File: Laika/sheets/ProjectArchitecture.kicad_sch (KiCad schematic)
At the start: 0 parts

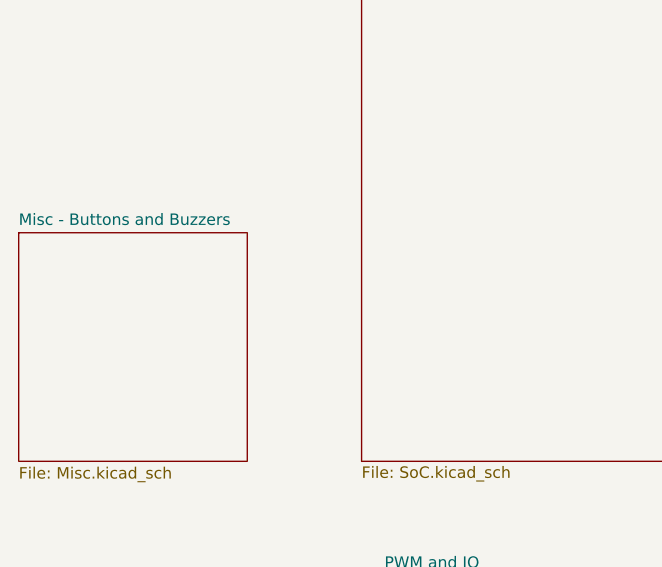
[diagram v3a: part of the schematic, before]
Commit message: Created misc. block
Populated sheet for misc. components. This includes three switches for
SoC bringup (update, reset, arm/risc-v select). Added buzzer and user
led.
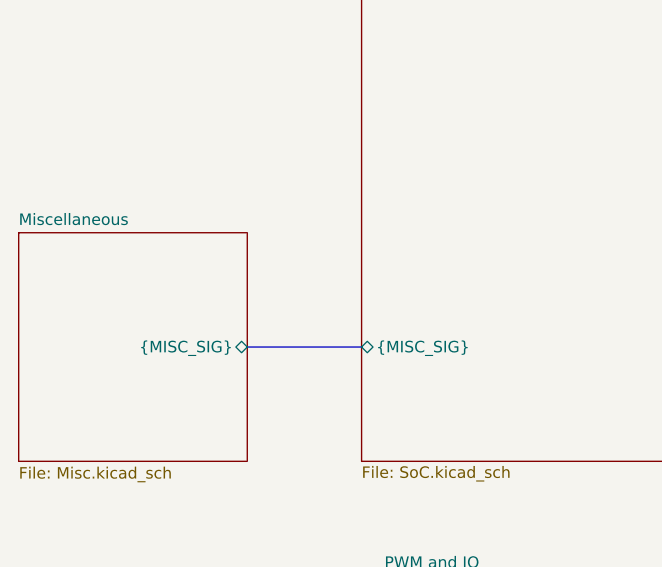
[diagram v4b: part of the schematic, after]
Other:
- sheet Misc - Buttons and Buzzers renamed Miscellaneous
- sheet Miscellaneous ports: added {MISC_SIG}; removed none
- sheet SoC ports: added {MISC_SIG}; removed none
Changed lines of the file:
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@@
+		)
+	)
+	(bus
+		(pts
+			(xy 63.5 127) (xy 76.2 127)
+		)
+		(stroke
+			(width 0)
+			(type default)
 		)
 	)
@@
 			(color 212 212 199 1.0000)
 		)
-		(property "Sheetname" "Misc - Buttons and Buzzers"
+		(property "Sheetname" "Miscellaneous"
 			(at 38.1 113.5884 0)
 			(effects
@@
 			)
 		)
+		(pin "{MISC_SIG}" bidirectional
+			(at 63.5 127 0)
+			(effects
+				(font
+					(size 1.27 1.27)
+				)
+				(justify right)
+			)
+		)
 		(instances
 			(project "Laika"
@@
 			(effects
 				(font
+					(size 1.27 1.27)
+				)
+				(justify left)
+			)
+		)
+		(pin "{MISC_SIG}" bidirectional
+			(at 76.2 127 180)
+			(effects
+				(font

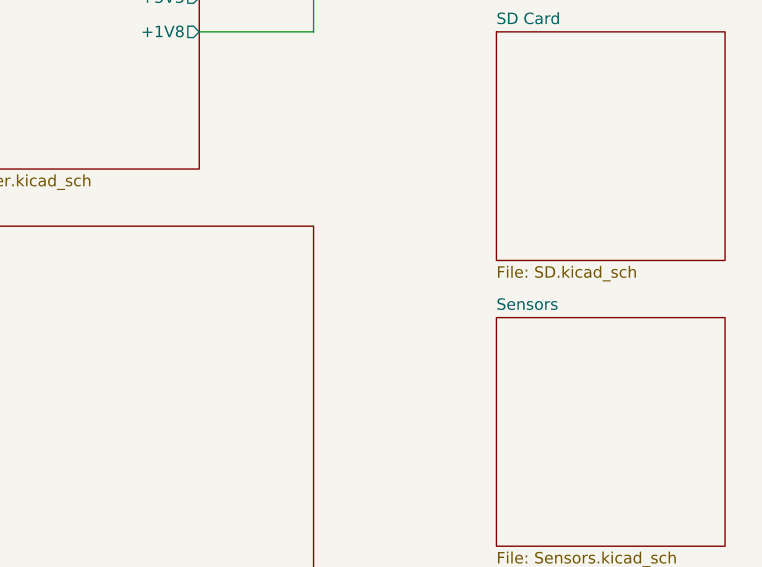
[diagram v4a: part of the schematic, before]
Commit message: Added SD card power source selector and boot medium selector.
The SD card power source (VDD_SD) can be selected between a software
managed 3.3V power supply (PWR_SD_SW); or through the 3.3V power rail
(+3V3). Doubles as selector whether to boot from SD card or eMMC.
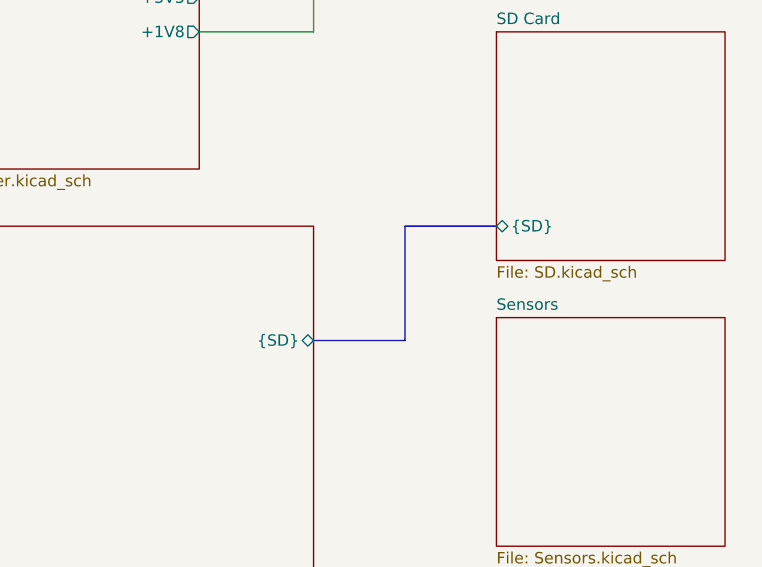
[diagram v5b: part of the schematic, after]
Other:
- sheet SD Card ports: added {SD}; removed none
- sheet SoC ports: added {SD}; removed none
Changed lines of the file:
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@@
 		(comment 1 "${VARIANT}")
 	)
+	(bus
+		(pts
+			(xy 149.86 50.8) (xy 160.02 50.8)
+		)
+		(stroke
+			(width 0)
+			(type default)
+		)
+	)
 	(wire
 		(pts
@@
 	(bus
 		(pts
+			(xy 139.7 63.5) (xy 149.86 63.5)
+		)
+		(stroke
+			(width 0)
+			(type default)
+		)
+	)
+	(bus
+		(pts
 			(xy 76.2 63.5) (xy 69.85 63.5)
 		)
@@
 		(pts
 			(xy 69.85 38.1) (xy 63.5 38.1)
+		)
+		(stroke
+			(width 0)
+			(type default)
+		)
+	)
+	(bus
+		(pts
+			(xy 149.86 63.5) (xy 149.86 50.8)
 		)
 		(stroke
@@
 			)
 		)
+		(pin "{SD}" bidirectional
+			(at 160.02 50.8 180)
+			(effects
+				(font
+					(size 1.27 1.27)
+				)
+				(justify left)
+			)
+		)
 		(instances
 			(project "Laika"
@@
 			)
 		)
+		(pin "{SD}" bidirectional
+			(at 139.7 63.5 0)
+			(effects
+				(font
+					(size 1.27 1.27)
+				)
+				(justify right)
+			)
+		)

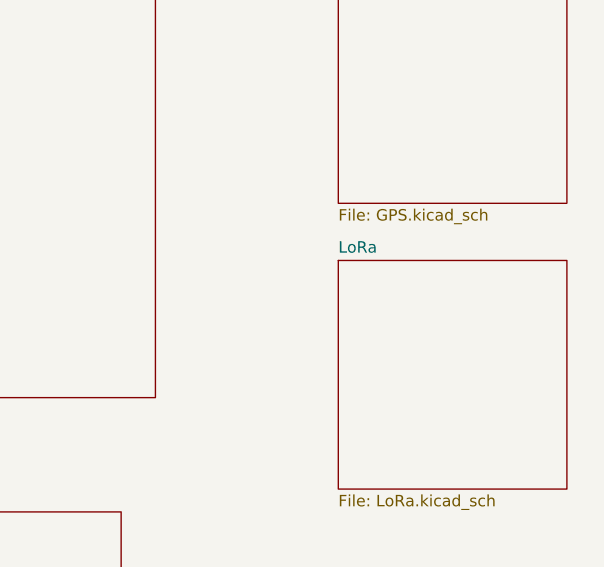
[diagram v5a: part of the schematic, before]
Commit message: Created schematic for Reyax RYLR993 LoRa module
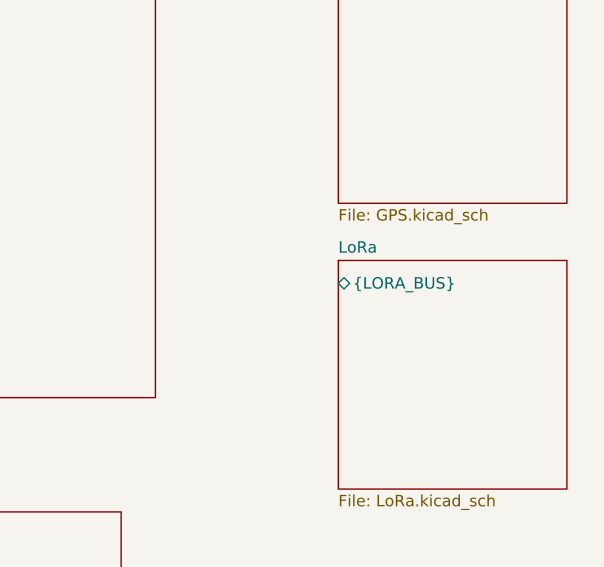
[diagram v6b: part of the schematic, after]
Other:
- sheet LoRa ports: added {LORA_BUS}; removed none
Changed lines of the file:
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@@
+			)
+		)
+		(pin "{LORA_BUS}" bidirectional
+			(at 160.02 127 180)
+			(effects
+				(font
+					(size 1.27 1.27)
+				)
+				(justify left)
 			)
 		)

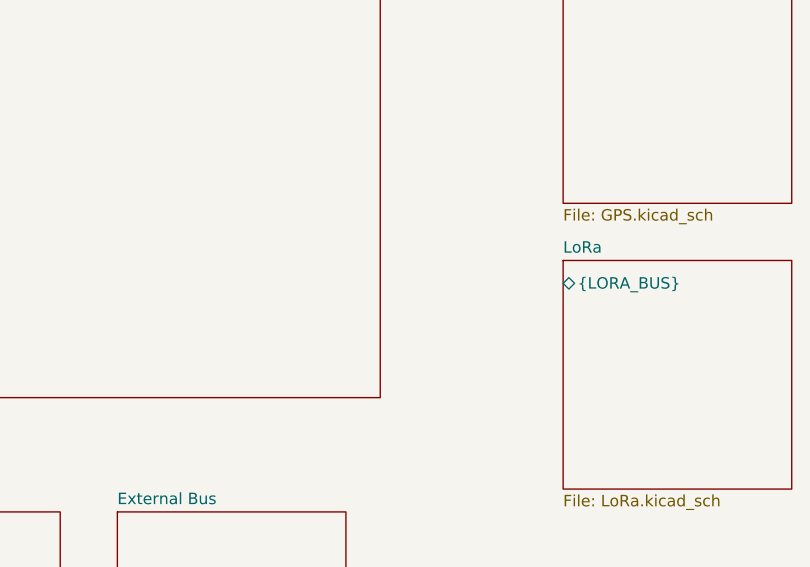
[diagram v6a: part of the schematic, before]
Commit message: Connected LoRa module to UART1 with reset
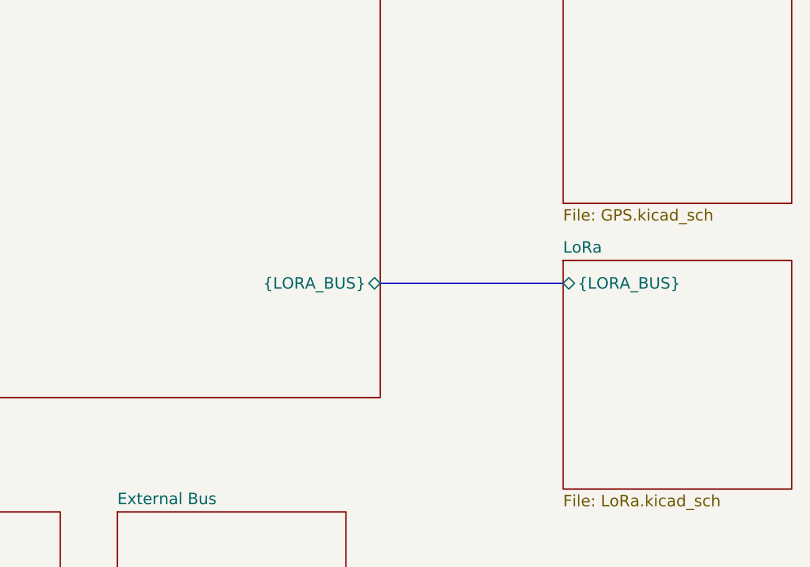
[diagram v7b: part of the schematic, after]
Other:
- sheet SoC ports: added {LORA_BUS}; removed none
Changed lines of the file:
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@@
+	(bus
+		(pts
+			(xy 139.7 127) (xy 160.02 127)
+		)
+		(stroke
+			(width 0)
+			(type default)
+		)
+	)
 	(bus
 		(pts
@@
 			(effects
 				(font
+					(size 1.27 1.27)
+				)
+				(justify right)
+			)
+		)
+		(pin "{LORA_BUS}" bidirectional
+			(at 139.7 127 0)
+			(effects
+				(font

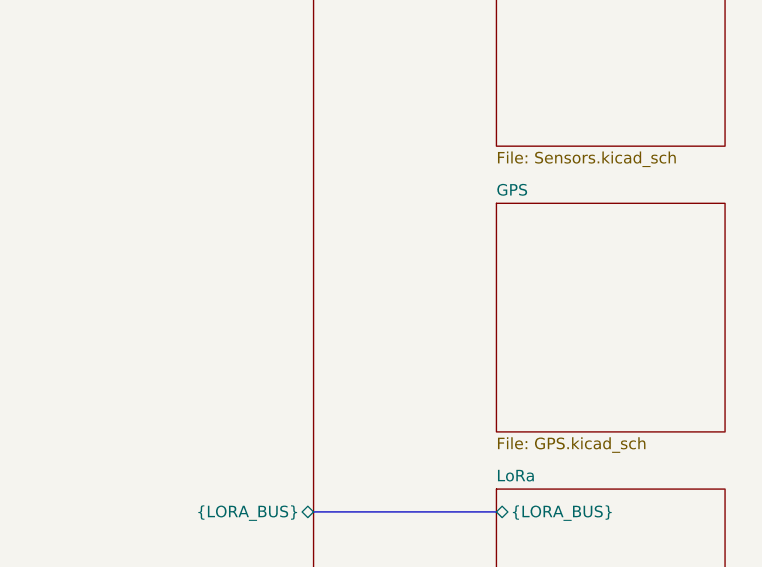
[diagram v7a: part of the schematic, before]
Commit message: Connected GPS to UART2.
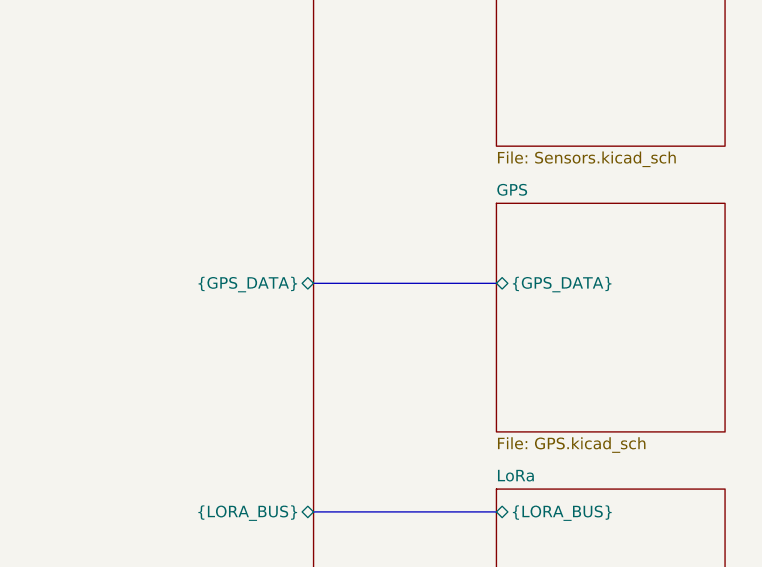
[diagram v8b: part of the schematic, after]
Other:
- sheet GPS ports: added {GPS_DATA}; removed none
- sheet SoC ports: added {GPS_DATA}; removed none
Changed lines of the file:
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@@
+		)
+	)
+	(bus
+		(pts
+			(xy 139.7 101.6) (xy 160.02 101.6)
+		)
+		(stroke
+			(width 0)
+			(type default)
 		)
 	)
@@
 			)
 		)
+		(pin "{GPS_DATA}" bidirectional
+			(at 160.02 101.6 180)
+			(effects
+				(font
+					(size 1.27 1.27)
+				)
+				(justify left)
+			)
+		)
 		(instances
 			(project "Laika"
@@
 			(effects
 				(font
+					(size 1.27 1.27)
+				)
+				(justify right)
+			)
+		)
+		(pin "{GPS_DATA}" bidirectional
+			(at 139.7 101.6 0)
+			(effects
+				(font
